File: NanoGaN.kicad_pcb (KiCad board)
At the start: 2 copper layers, 52 parts, among them J1 U_DC, J10 Conn_01x06, J11 Conn_01x04, J12 USB4085-GF-A, J2 GND, J3 Phase_U, J4 Phase_V, J5 Phase_W, J6 FTSH-107-01-L-DV-K-TR, J7 Conn_01x03, J9 Conn_01x07, Q1 IGC025S08S1, Q2 IGC025S08S1, Q3 IGC025S08S1, Q4 IGC025S08S1, Q5 IGC025S08S1, Q6 IGC025S08S1, U1 STM32H723VGTx, U10 LMG1205YFXR, U12 AD8418, U13 BMI323, U14 AS5047P-ATST, U15 TCAN1044VDRQ1, U2 LMR51635XDDCR, U3 AMS1117, U4 AD8418, U7 LMG1205YFXR, U9 AD8418, X1 8MHz

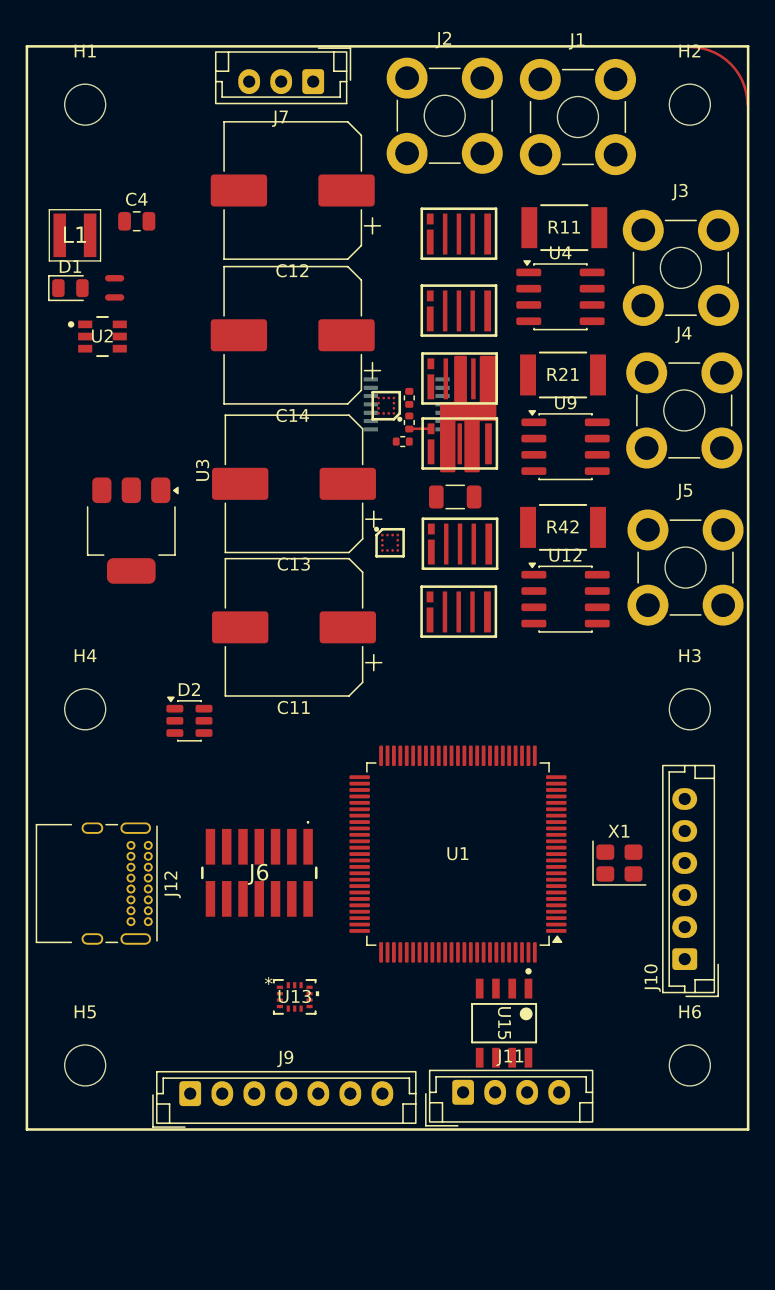
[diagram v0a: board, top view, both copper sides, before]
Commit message: Updated the DC/DC converter from I_out = 2A to 3.5A  and fsw = 1.1MHz to 400kHz
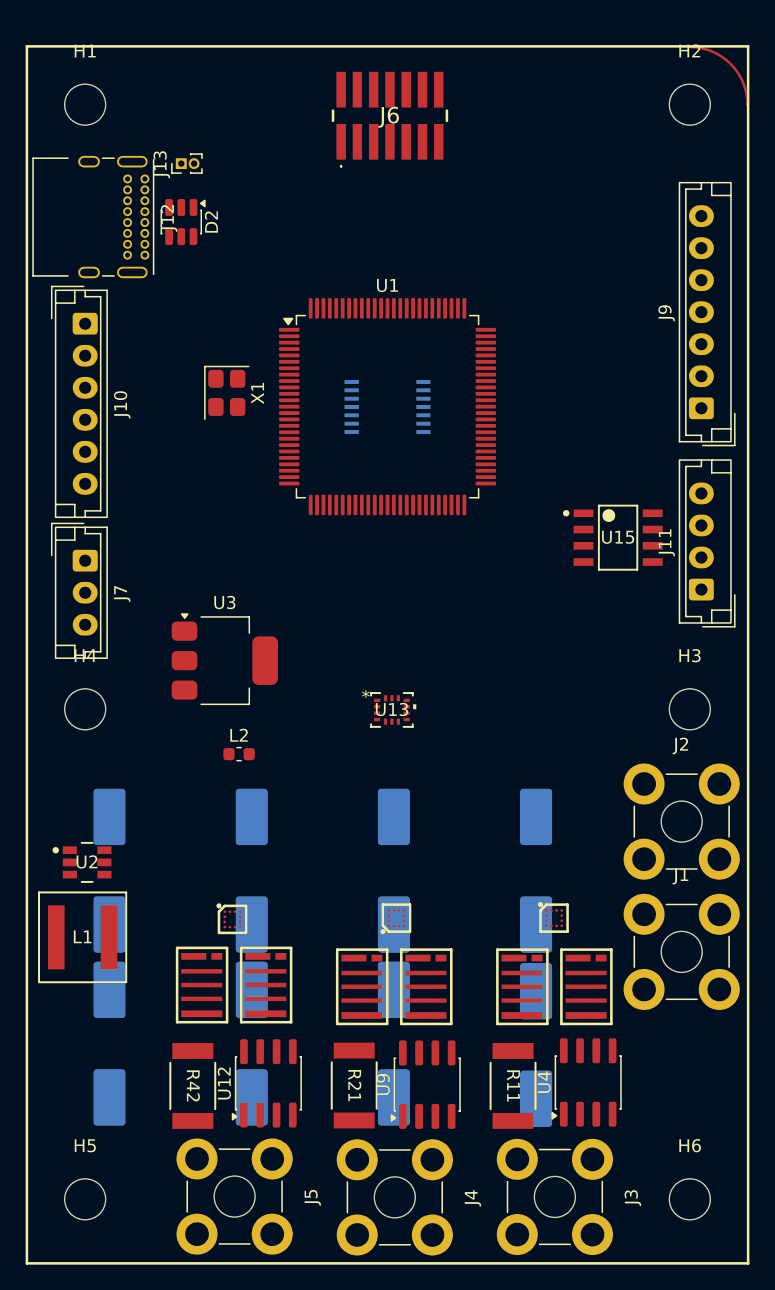
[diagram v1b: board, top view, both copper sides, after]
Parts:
- removed C4: 100n, Capacitor_SMD:C_0805_2012Metric
- removed C48: 1u, Capacitor_SMD:C_1206_3216Metric
- removed D1: RED, LED_SMD:LED_0805_2012Metric
- removed NT1, NT2: NetTie_2, NetTie:NetTie-2_SMD_Pad0.5mm
- removed R17, R18: 1, Resistor_SMD:R_0402_1005Metric
- removed R20: 39k, Resistor_SMD:R_0402_1005Metric
- added C27: 150u, Capacitor_SMD:CP_Elec_10x10.5, B.Cu at (21.9, 93.3)
- added C35: 150u, Capacitor_SMD:CP_Elec_10x10.5, B.Cu at (33.0, 93.3)
- added C44: 150u, Capacitor_SMD:CP_Elec_10x10.5, B.Cu at (44.1, 93.3)
- added C81: 150u, Capacitor_SMD:CP_Elec_10x10.5, B.Cu at (55.2, 93.4)
- added J13: Conn_01x02, Connector_PinHeader_1.00mm:PinHeader_1x02_P1.00mm_Vertical, F.Cu at (27.5, 24.6)
- added L2: 39n, Inductor_SMD:L_0603_1608Metric, F.Cu at (32.0, 70.7)
- added U5: LMG1205YFXR, NanoGaN:BGA12C40P4X4_173X188X68, F.Cu at (56.6, 83.5)
- C11, C12, C13, C14: moved to B.Cu
- L1: value 3u3 -> 10u; footprint NanoGaN:XAL40XX -> NanoGaN:IND_XAL60XX-240H_COC
- moved J3 73.2 mm to (56.7, 105.3), turned to -90 degrees
- moved J10 68.2 mm to (20.0, 37.1), turned to -90 degrees
- moved R11 67.1 mm to (53.4, 96.6), turned to -90 degrees
- moved J9 66.7 mm to (68.1, 43.7), turned to 90 degrees
- moved J1 65.7 mm to (66.6, 86.1)
- moved J4 65.5 mm to (44.2, 105.3), turned to -90 degrees
- moved U4 61.4 mm to (59.3, 96.3), turned to 90 degrees
- moved J5 60.4 mm to (31.7, 105.2), turned to -90 degrees
- moved J6 60.0 mm to (43.8, 20.9), turned to 0 degrees
- moved Q1 59.3 mm to (54.4, 88.9), turned to -90 degrees
- moved J2 58.1 mm to (66.6, 76.0)
- moved R21 57.8 mm to (41.0, 96.6), turned to -90 degrees
- moved C12 56.4 mm to (55.2, 79.8), turned to -90 degrees
- moved L1 54.8 mm to (19.8, 85.0)
- moved Q2 54.0 mm to (59.4, 88.9), turned to -90 degrees
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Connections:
- D2 pad 4: Net-(D2-I/O2-Pad4) -> /Connectors/D+
- D2 pad 6: Net-(D2-I/O1-Pad6) -> /Connectors/D-
- J12 pad A5: unconnected-(J12-CC1-PadA5) -> Net-(J12-CC1)
- J12 pad A6: Net-(D2-I/O2-Pad4) -> /Connectors/D+
- J12 pad A7: Net-(D2-I/O1-Pad6) -> /Connectors/D-
- J12 pad B5: unconnected-(J12-CC2-PadB5) -> Net-(J12-CC2)
- J12 pad B6: Net-(D2-I/O2-Pad4) -> /Connectors/D+
- J12 pad B7: Net-(D2-I/O1-Pad6) -> /Connectors/D-
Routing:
- net /HalfBridgeV/LOL: track 1.70 -> 0.00 mm
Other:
- board text added: "${REFERENCE}"

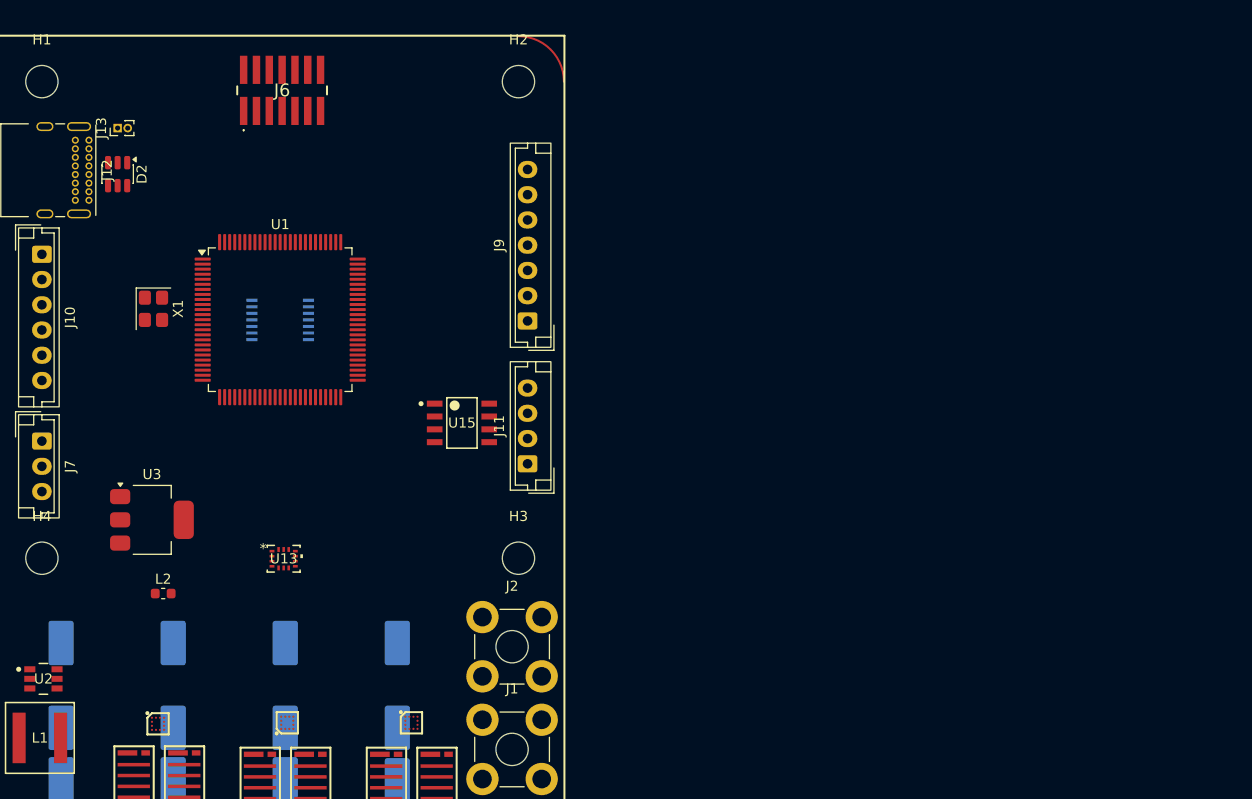
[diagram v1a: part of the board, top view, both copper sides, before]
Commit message: added cooling channel trace on F silkscreen and rearranged a few components
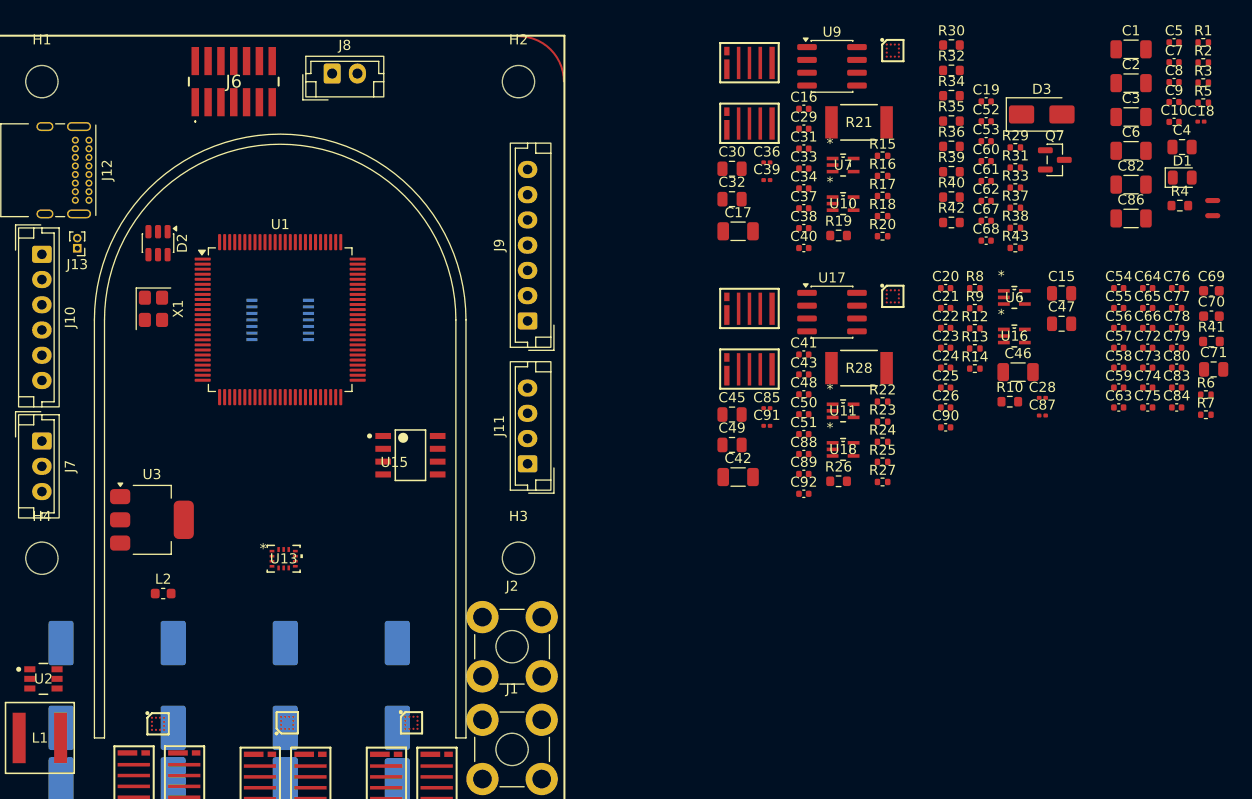
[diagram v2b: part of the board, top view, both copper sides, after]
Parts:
- added C1: 1u, Capacitor_SMD:C_1206_3216Metric, F.Cu at (127.9, 16.8)
- added C10: 100n, Capacitor_SMD:C_0402_1005Metric, F.Cu at (132.1, 24.0)
- added C15: 100n, Capacitor_SMD:C_0805_2012Metric, F.Cu at (121.0, 41.0)
- added C16: 1u, Capacitor_SMD:C_0402_1005Metric, F.Cu at (95.5, 22.7)
- added C17: 1u, Capacitor_SMD:C_1206_3216Metric, F.Cu at (89.0, 34.8)
- added C18: 1n, Capacitor_SMD:C_0201_0603Metric, F.Cu at (134.8, 24.0)
- added C19: 4.7n, Capacitor_SMD:C_0402_1005Metric, F.Cu at (113.5, 22.0)
- added C2: 1u, Capacitor_SMD:C_1206_3216Metric, F.Cu at (127.9, 20.1)
- added C20: 1u, Capacitor_SMD:C_0402_1005Metric, F.Cu at (109.5, 40.5)
- added C21: 100n, Capacitor_SMD:C_0402_1005Metric, F.Cu at (109.5, 42.4)
- added C22: 100n, Capacitor_SMD:C_0402_1005Metric, F.Cu at (109.5, 44.4)
- added C23: 100n, Capacitor_SMD:C_0402_1005Metric, F.Cu at (109.5, 46.4)
- added C24: 100n, Capacitor_SMD:C_0402_1005Metric, F.Cu at (109.5, 48.3)
- added C25: 100n, Capacitor_SMD:C_0402_1005Metric, F.Cu at (109.5, 50.3)
- added C26: 1u, Capacitor_SMD:C_0402_1005Metric, F.Cu at (109.5, 52.3)
- added C28: 1n, Capacitor_SMD:C_0201_0603Metric, F.Cu at (119.1, 51.3)
- added C29: 100n, Capacitor_SMD:C_0402_1005Metric, F.Cu at (95.5, 24.7)
- added C3: 1u, Capacitor_SMD:C_1206_3216Metric, F.Cu at (127.9, 23.5)
- added C30: 100n, Capacitor_SMD:C_0805_2012Metric, F.Cu at (88.3, 28.6)
- added C31: 100n, Capacitor_SMD:C_0402_1005Metric, F.Cu at (95.5, 26.6)
- added C32: 100n, Capacitor_SMD:C_0805_2012Metric, F.Cu at (88.3, 31.6)
- added C33: 100n, Capacitor_SMD:C_0402_1005Metric, F.Cu at (95.5, 28.6)
- added C34: 100n, Capacitor_SMD:C_0402_1005Metric, F.Cu at (95.5, 30.6)
- added C36: 1n, Capacitor_SMD:C_0201_0603Metric, F.Cu at (91.8, 28.0)
- added C37: 1u, Capacitor_SMD:C_0402_1005Metric, F.Cu at (95.5, 32.5)
- added C38: 100n, Capacitor_SMD:C_0402_1005Metric, F.Cu at (95.5, 34.5)
- added C39: 1n, Capacitor_SMD:C_0201_0603Metric, F.Cu at (91.8, 29.8)
- added C4: 100n, Capacitor_SMD:C_0805_2012Metric, F.Cu at (132.9, 26.5)
- added C40: 15n, Capacitor_SMD:C_0402_1005Metric, F.Cu at (95.5, 36.5)
- added C41: 1u, Capacitor_SMD:C_0402_1005Metric, F.Cu at (95.5, 47.0)
- added C42: 1u, Capacitor_SMD:C_1206_3216Metric, F.Cu at (89.0, 59.2)
- added C43: 100n, Capacitor_SMD:C_0402_1005Metric, F.Cu at (95.5, 49.0)
- added C45: 100n, Capacitor_SMD:C_0805_2012Metric, F.Cu at (88.3, 53.0)
- added C46: 1u, Capacitor_SMD:C_1206_3216Metric, F.Cu at (116.7, 48.8)
- added C47: 100n, Capacitor_SMD:C_0805_2012Metric, F.Cu at (121.0, 44.0)
- added C48: 100n, Capacitor_SMD:C_0402_1005Metric, F.Cu at (95.5, 51.0)
- added C49: 100n, Capacitor_SMD:C_0805_2012Metric, F.Cu at (88.3, 56.0)
- added C5: 100n, Capacitor_SMD:C_0402_1005Metric, F.Cu at (132.1, 16.1)
- added C50: 100n, Capacitor_SMD:C_0402_1005Metric, F.Cu at (95.5, 52.9)
- added C51: 100n, Capacitor_SMD:C_0402_1005Metric, F.Cu at (95.5, 54.9)
- added C52: 1u, Capacitor_SMD:C_0402_1005Metric, F.Cu at (113.5, 23.9)
- added C53: 1u, Capacitor_SMD:C_0402_1005Metric, F.Cu at (113.5, 25.9)
- added C54: 1u, Capacitor_SMD:C_0402_1005Metric, F.Cu at (126.7, 40.5)
- added C55: 100n, Capacitor_SMD:C_0402_1005Metric, F.Cu at (126.7, 42.4)
- added C56: 100n, Capacitor_SMD:C_0402_1005Metric, F.Cu at (126.7, 44.4)
- added C57: 100n, Capacitor_SMD:C_0402_1005Metric, F.Cu at (126.7, 46.4)
- added C58: 1u, Capacitor_SMD:C_0402_1005Metric, F.Cu at (126.7, 48.3)
- added C59: 100n, Capacitor_SMD:C_0402_1005Metric, F.Cu at (126.7, 50.3)
- added C6: 47u, Capacitor_SMD:C_1206_3216Metric, F.Cu at (127.9, 26.9)
- added C60: 4.7n, Capacitor_SMD:C_0402_1005Metric, F.Cu at (113.5, 27.9)
- added C61: 4.7n, Capacitor_SMD:C_0402_1005Metric, F.Cu at (113.5, 29.8)
- added C62: 4.7n, Capacitor_SMD:C_0402_1005Metric, F.Cu at (113.5, 31.8)
- added C63: 1u, Capacitor_SMD:C_0402_1005Metric, F.Cu at (126.7, 52.3)
- added C64: 100n, Capacitor_SMD:C_0402_1005Metric, F.Cu at (129.5, 40.5)
- added C65: 1u, Capacitor_SMD:C_0402_1005Metric, F.Cu at (129.5, 42.4)
- added C66: 100n, Capacitor_SMD:C_0402_1005Metric, F.Cu at (129.5, 44.4)
- added C67: 1u, Capacitor_SMD:C_0402_1005Metric, F.Cu at (113.5, 33.8)
- added C68: 1u, Capacitor_SMD:C_0402_1005Metric, F.Cu at (113.5, 35.8)
- added C69: 18p, Capacitor_SMD:C_0603_1608Metric, F.Cu at (135.8, 40.7)
- added C7: 4u7, Capacitor_SMD:C_0402_1005Metric, F.Cu at (132.1, 18.1)
- added C70: 18p, Capacitor_SMD:C_0603_1608Metric, F.Cu at (135.8, 43.2)
- added C71: 10u, Capacitor_SMD:C_0805_2012Metric, F.Cu at (136.1, 48.5)
- added C72: 1u, Capacitor_SMD:C_0402_1005Metric, F.Cu at (129.5, 46.4)
- added C73: 100n, Capacitor_SMD:C_0402_1005Metric, F.Cu at (129.5, 48.3)
- added C74: 100n, Capacitor_SMD:C_0402_1005Metric, F.Cu at (129.5, 50.3)
- added C75: 100n, Capacitor_SMD:C_0402_1005Metric, F.Cu at (129.5, 52.3)
- added C76: 100n, Capacitor_SMD:C_0402_1005Metric, F.Cu at (132.4, 40.5)
- added C77: 100n, Capacitor_SMD:C_0402_1005Metric, F.Cu at (132.4, 42.4)
- added C78: 100n, Capacitor_SMD:C_0402_1005Metric, F.Cu at (132.4, 44.4)
- added C79: 100n, Capacitor_SMD:C_0402_1005Metric, F.Cu at (132.4, 46.4)
- added C8: 4u7, Capacitor_SMD:C_0402_1005Metric, F.Cu at (132.1, 20.1)
- added C80: 100n, Capacitor_SMD:C_0402_1005Metric, F.Cu at (132.4, 48.3)
- added C82: 47u, Capacitor_SMD:C_1206_3216Metric, F.Cu at (127.9, 30.2)
- added C83: 2u2, Capacitor_SMD:C_0402_1005Metric, F.Cu at (132.4, 50.3)
- added C84: 2u2, Capacitor_SMD:C_0402_1005Metric, F.Cu at (132.4, 52.3)
- added C85: 1n, Capacitor_SMD:C_0201_0603Metric, F.Cu at (91.8, 52.3)
- added C86: 47u, Capacitor_SMD:C_1206_3216Metric, F.Cu at (127.9, 33.5)
- added C87: 1n, Capacitor_SMD:C_0201_0603Metric, F.Cu at (119.1, 53.1)
- added C88: 1u, Capacitor_SMD:C_0402_1005Metric, F.Cu at (95.5, 56.9)
- added C89: 100n, Capacitor_SMD:C_0402_1005Metric, F.Cu at (95.5, 58.9)
- added C9: 1u, Capacitor_SMD:C_0402_1005Metric, F.Cu at (132.1, 22.0)
- added C90: 15n, Capacitor_SMD:C_0402_1005Metric, F.Cu at (109.5, 54.2)
- added C91: 1n, Capacitor_SMD:C_0201_0603Metric, F.Cu at (91.8, 54.1)
- added C92: 15n, Capacitor_SMD:C_0402_1005Metric, F.Cu at (95.5, 60.8)
- added D1: RED, LED_SMD:LED_0805_2012Metric, F.Cu at (132.9, 29.5)
- added D3: SS54, Diode_SMD:D_SMA, F.Cu at (119.0, 23.2)
- added J8: Conn_01x02, Connector_JST:JST_EH_B2B-EH-A_1x02_P2.50mm_Vertical, F.Cu at (48.8, 19.2)
- added NT1: NetTie_2, NetTie:NetTie-2_SMD_Pad0.5mm, F.Cu at (136.0, 31.8)
- added NT2: NetTie_2, NetTie:NetTie-2_SMD_Pad0.5mm, F.Cu at (136.0, 33.3)
- added Q3: IGC025S08S1, NanoGaN:IFX-PG-TSON-6-2-V, F.Cu at (90.1, 17.9)
- added Q4: IGC025S08S1, NanoGaN:IFX-PG-TSON-6-2-V, F.Cu at (90.1, 23.9)
- added Q5: IGC025S08S1, NanoGaN:IFX-PG-TSON-6-2-V, F.Cu at (90.1, 42.2)
- added Q6: IGC025S08S1, NanoGaN:IFX-PG-TSON-6-2-V, F.Cu at (90.1, 48.2)
- added Q7: Si2302CDS, NanoGaN:SOT-23_Si2302CDS, F.Cu at (120.3, 27.8)
- added R1: 100k, Resistor_SMD:R_0402_1005Metric, F.Cu at (135.0, 16.1)
- added R10: 39k, Resistor_SMD:R_0603_1608Metric, F.Cu at (115.9, 51.7)
- added R12: 2k2, Resistor_SMD:R_0402_1005Metric, F.Cu at (112.4, 44.4)
- added R13: 39k, Resistor_SMD:R_0402_1005Metric, F.Cu at (112.4, 46.4)
- added R14: 39k, Resistor_SMD:R_0402_1005Metric, F.Cu at (112.4, 48.4)
- added R15: 1, Resistor_SMD:R_0402_1005Metric, F.Cu at (103.3, 27.4)
- added R16: 1, Resistor_SMD:R_0402_1005Metric, F.Cu at (103.3, 29.3)
- added R17: 39k, Resistor_SMD:R_0402_1005Metric, F.Cu at (103.3, 31.3)
- added R18: 39k, Resistor_SMD:R_0402_1005Metric, F.Cu at (103.3, 33.3)
- added R19: 39k, Resistor_SMD:R_0603_1608Metric, F.Cu at (98.9, 35.2)
- added R2: 19.1k, Resistor_SMD:R_0402_1005Metric, F.Cu at (135.0, 18.1)
- added R20: 2k2, Resistor_SMD:R_0402_1005Metric, F.Cu at (103.3, 35.3)
- added R21: 1m, NanoGaN:RES_00FEA_VIS-L, F.Cu at (100.9, 24.0)
- added R22: 1, Resistor_SMD:R_0402_1005Metric, F.Cu at (103.3, 51.7)
- added R23: 1, Resistor_SMD:R_0402_1005Metric, F.Cu at (103.3, 53.7)
- added R24: 39k, Resistor_SMD:R_0402_1005Metric, F.Cu at (103.3, 55.7)
- added R25: 39k, Resistor_SMD:R_0402_1005Metric, F.Cu at (103.3, 57.7)
- added R26: 39k, Resistor_SMD:R_0603_1608Metric, F.Cu at (98.9, 59.6)
- added R27: 2k2, Resistor_SMD:R_0402_1005Metric, F.Cu at (103.3, 59.6)
- added R28: 1m, NanoGaN:RES_00FEA_VIS-L, F.Cu at (100.9, 48.4)
- added R29: 2k2, Resistor_SMD:R_0402_1005Metric, F.Cu at (116.4, 26.5)
- added R3: 220, Resistor_SMD:R_0402_1005Metric, F.Cu at (135.0, 20.1)
- added R30: 10k, Resistor_SMD:R_0603_1608Metric, F.Cu at (110.1, 16.4)
- added R31: 2k2, Resistor_SMD:R_0402_1005Metric, F.Cu at (116.4, 28.5)
- added R32: 10k, Resistor_SMD:R_0603_1608Metric, F.Cu at (110.1, 18.9)
- added R33: 2k2, Resistor_SMD:R_0402_1005Metric, F.Cu at (116.4, 30.5)
- added R34: 10k, Resistor_SMD:R_0603_1608Metric, F.Cu at (110.1, 21.4)
- added R35: 10k, Resistor_SMD:R_0603_1608Metric, F.Cu at (110.1, 23.9)
- added R36: 10k, Resistor_SMD:R_0603_1608Metric, F.Cu at (110.1, 26.4)
- added R37: 5k1, Resistor_SMD:R_0402_1005Metric, F.Cu at (116.4, 32.5)
- added R38: 5k1, Resistor_SMD:R_0402_1005Metric, F.Cu at (116.4, 34.5)
- added R39: 0R, Resistor_SMD:R_0603_1608Metric, F.Cu at (110.1, 28.9)
- added R4: 39k, Resistor_SMD:R_0603_1608Metric, F.Cu at (132.7, 32.3)
- added R40: 0R, Resistor_SMD:R_0603_1608Metric, F.Cu at (110.1, 31.4)
- added R41: 10k, Resistor_SMD:R_0603_1608Metric, F.Cu at (135.8, 45.7)
- added R42: 10k, Resistor_SMD:R_0603_1608Metric, F.Cu at (110.1, 34.0)
- added R43: 100, Resistor_SMD:R_0402_1005Metric, F.Cu at (116.4, 36.5)
- added R5: 2k2, Resistor_SMD:R_0402_1005Metric, F.Cu at (135.0, 22.1)
- added R6: 120, Resistor_SMD:R_0402_1005Metric, F.Cu at (135.3, 51.0)
- added R7: 0, Resistor_SMD:R_0402_1005Metric, F.Cu at (135.3, 53.0)
- added R8: 1, Resistor_SMD:R_0402_1005Metric, F.Cu at (112.4, 40.5)
- added R9: 1, Resistor_SMD:R_0402_1005Metric, F.Cu at (112.4, 42.5)
- added U10: SN74LVC1G66DCKR, NanoGaN:DCK5, F.Cu at (99.4, 32.1)
- added U11: SN74LVC1G66DCKR, NanoGaN:DCK5, F.Cu at (99.4, 52.6)
- added U12: LMG1205YFXR, NanoGaN:BGA12C40P4X4_173X188X68, F.Cu at (104.3, 41.3)
- added U16: SN74LVC1G66DCKR, NanoGaN:DCK5, F.Cu at (116.3, 45.2)
- added U17: AD8418, Package_SO:SOIC-8_3.9x4.9mm_P1.27mm, F.Cu at (98.2, 42.8)
- added U18: SN74LVC1G66DCKR, NanoGaN:DCK5, F.Cu at (99.4, 56.4)
- added U6: SN74LVC1G66DCKR, NanoGaN:DCK5, F.Cu at (116.3, 41.4)
- added U7: SN74LVC1G66DCKR, NanoGaN:DCK5, F.Cu at (99.4, 28.3)
- added U8: LMG1205YFXR, NanoGaN:BGA12C40P4X4_173X188X68, F.Cu at (104.3, 16.9)
- added U9: AD8418, Package_SO:SOIC-8_3.9x4.9mm_P1.27mm, F.Cu at (98.2, 18.5)
- moved J13 12.6 mm to (23.5, 36.5), turned to 180 degrees
- moved D2 7.92 mm to (31.5, 36.0)
- moved U15 6.02 mm to (56.5, 57.0)
- moved J6 4.87 mm to (39.0, 20.0)
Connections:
- U1 pad 19: GNDA -> AGND
- U1 pad 37: /MCU/ENABLE_CURR_FILTER -> /HalfBridgeU/EN_FILTER_I
